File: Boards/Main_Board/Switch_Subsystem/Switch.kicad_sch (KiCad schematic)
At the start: 7 parts, among them U7 JS102011SCQN, U8 UCLAMP3301H.TCT

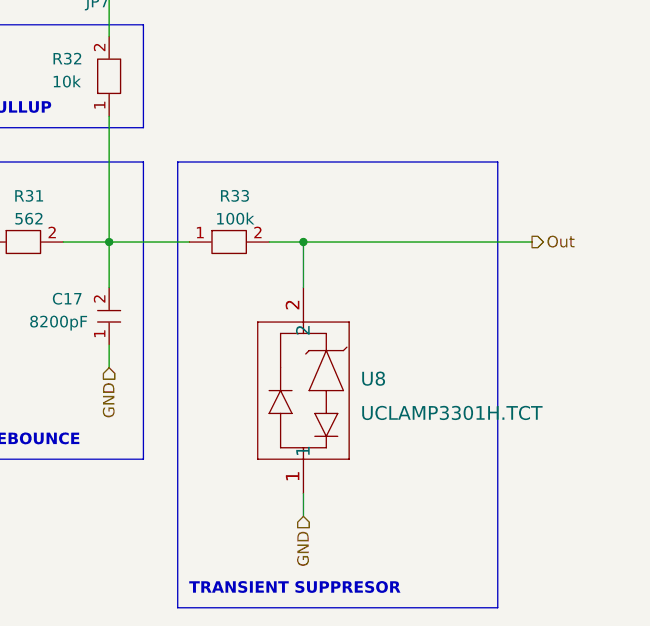
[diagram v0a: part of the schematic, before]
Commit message: Correct spacing on sensor board, refactor datasheets and project libraries
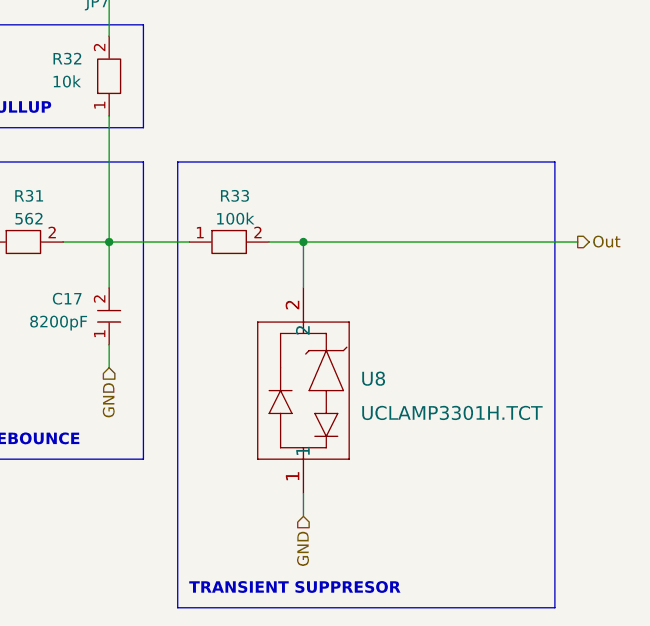
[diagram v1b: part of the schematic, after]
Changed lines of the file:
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@@
     (stroke (width 0) (type default) (color 0 0 0 0))
   )
-  (polyline (pts (xy 180.34 134.62) (xy 180.34 85.09))
+  (polyline (pts (xy 186.69 134.62) (xy 186.69 85.09))
     (stroke (width 0) (type default) (color 0 0 0 0))
   )
@@
     (stroke (width 0) (type default) (color 0 0 0 0))
   )
-  (wire (pts (xy 158.75 93.98) (xy 184.15 93.98))
+  (wire (pts (xy 158.75 93.98) (xy 189.23 93.98))
     (stroke (width 0) (type default) (color 0 0 0 0))
   )
@@
     (stroke (width 0) (type default) (color 0 0 0 0))
   )
-  (polyline (pts (xy 144.78 134.62) (xy 180.34 134.62))
+  (polyline (pts (xy 144.78 134.62) (xy 186.69 134.62))
     (stroke (width 0) (type default) (color 0 0 0 0))
   )
@@
     (stroke (width 0) (type default) (color 0 0 0 0))
   )
-  (polyline (pts (xy 144.78 85.09) (xy 180.34 85.09))
+  (polyline (pts (xy 144.78 85.09) (xy 186.69 85.09))
     (stroke (width 0) (type default) (color 0 0 0 0))
   )
@@
     (effects (font (size 1.27 1.27)) (justify right))
   )
-  (hierarchical_label "Out" (shape output) (at 184.15 93.98 0)
+  (hierarchical_label "Out" (shape output) (at 189.23 93.98 0)
     (effects (font (size 1.27 1.27)) (justify left))
   )
